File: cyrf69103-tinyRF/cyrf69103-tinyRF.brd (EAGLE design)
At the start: 19 x 13 mm, 32 parts

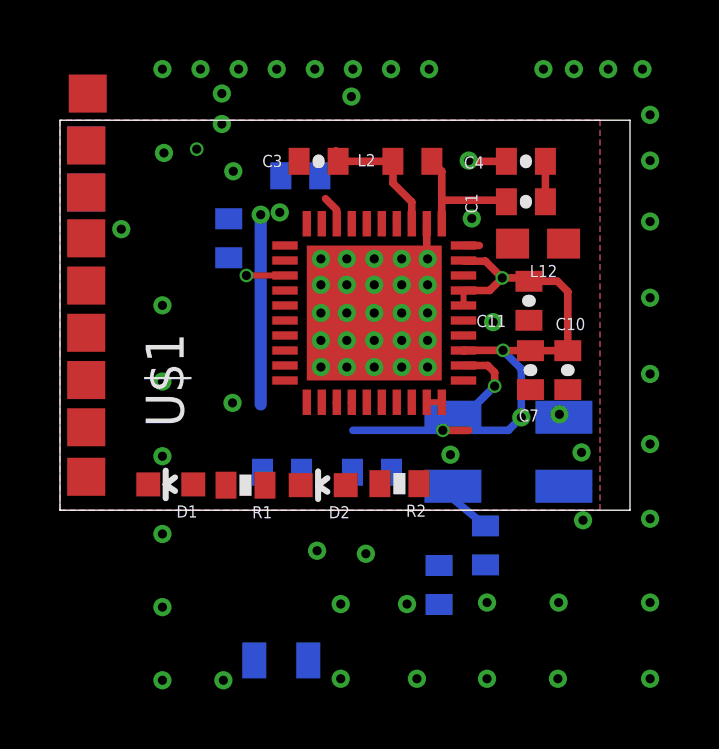
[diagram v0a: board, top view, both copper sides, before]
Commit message: Screwed up that last commit.  this update include changes to the production gerber folders.  Adds hackvana to the cyrf6936-BoB and cleans up the fab notes a bit.  Still need to standardize and parameterize the creation of the gerbers.
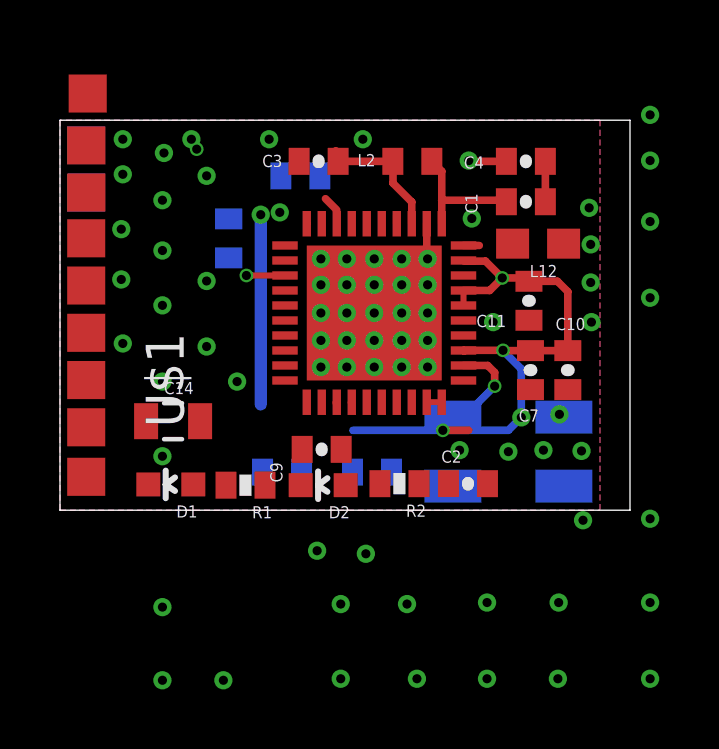
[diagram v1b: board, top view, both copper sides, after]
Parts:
- R1, R2: value (none) -> 330
- moved C14 8.75 mm to (10.8, 17.0), flipped to the top, turned to 180 degrees
- moved C9 5.98 mm to (15.7, 16.0), flipped to the top, turned to 180 degrees
- moved C2 2.14 mm to (20.6, 14.9), flipped to the top, turned to 0 degrees
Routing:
- net VDD_1.8: track 2.31 -> 0.00 mm
- net GND: vias 78 -> 77
